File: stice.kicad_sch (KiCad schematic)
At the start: 74 parts, among them SW1 SW_Push, SW10 SW_Push, SW11 SW_Push, SW12 SW_Push, SW13 SW_Push, SW14 SW_Push, SW15 SW_Push, SW16 SW_Push, SW17 SW_Push, SW18 SW_Push, SW19 SW_Push, SW2 SW_Push, SW20 SW_Push, SW21 SW_Push, SW22 SW_Push, SW23 SW_Push, SW24 SW_Push, SW25 SW_Push, SW26 SW_Push, SW27 SW_Push, SW28 SW_Push, SW29 SW_Push, SW3 SW_Push, SW30 SW_Push, SW31 SW_Push, SW32 SW_Push, SW33 SW_Push, SW34 SW_Push, SW35 SW_Push, SW36 SW_Push, SW37 SW_Push, SW4 SW_Push, SW5 SW_Push, SW6 SW_Push, SW7 SW_Push, SW8 SW_Push, SW9 SW_Push, U1 nice_nano

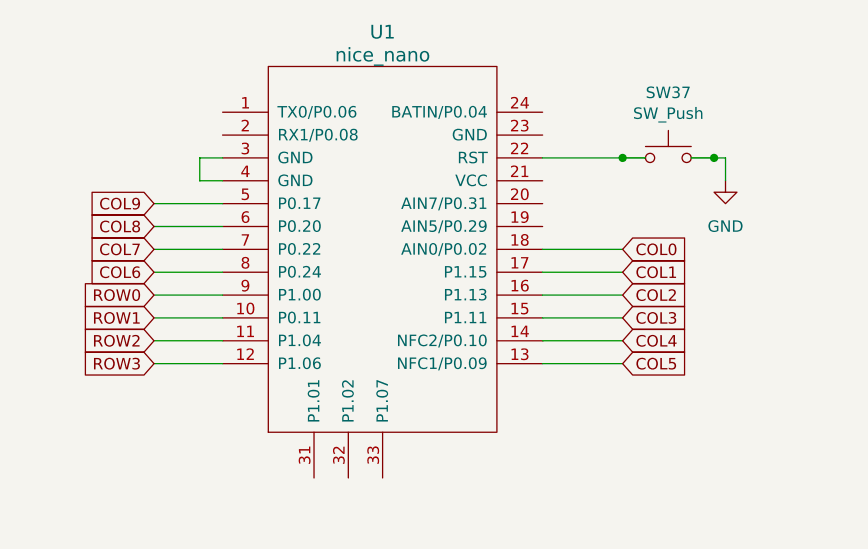
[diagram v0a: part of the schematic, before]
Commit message: outline done
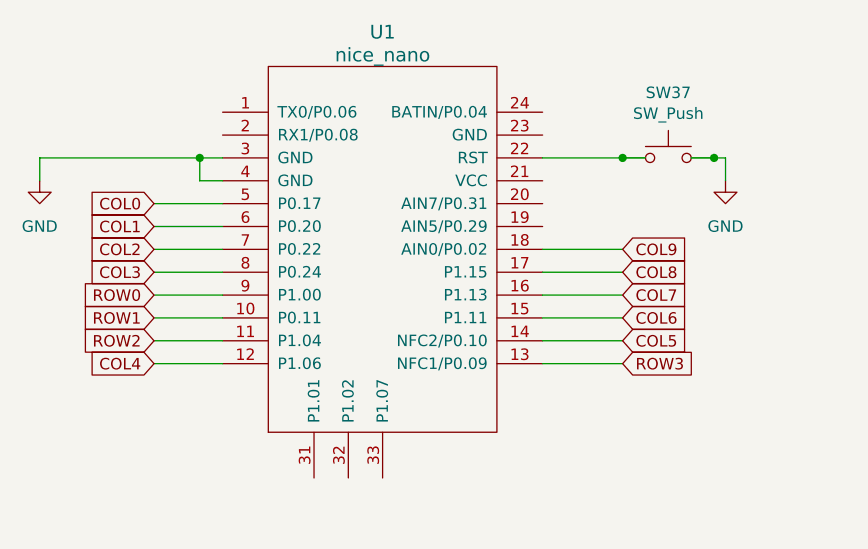
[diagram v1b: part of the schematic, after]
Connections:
- net COL0: now also U1.5 (P0.17); no longer U1.18 (AIN0/P0.02)
- net COL1: now also U1.6 (P0.20); no longer U1.17 (P1.15)
- net COL2: now also U1.7 (P0.22); no longer U1.16 (P1.13)
- net COL3: now also U1.8 (P0.24); no longer U1.15 (P1.11)
- net COL4: now also U1.12 (P1.06); no longer U1.14 (NFC2/P0.10)
- net COL5: now also U1.14 (NFC2/P0.10); no longer U1.13 (NFC1/P0.09)
- net COL6: now also U1.15 (P1.11); no longer U1.8 (P0.24)
- net COL7: now also U1.16 (P1.13); no longer U1.7 (P0.22)
- net COL8: now also U1.17 (P1.15); no longer U1.6 (P0.20)
- net COL9: now also U1.18 (AIN0/P0.02); no longer U1.5 (P0.17)
- net GND: now also U1.3 (GND), U1.4 (GND)
- net ROW3: now also U1.13 (NFC1/P0.09); no longer U1.12 (P1.06)
